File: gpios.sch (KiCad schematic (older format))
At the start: 13 parts

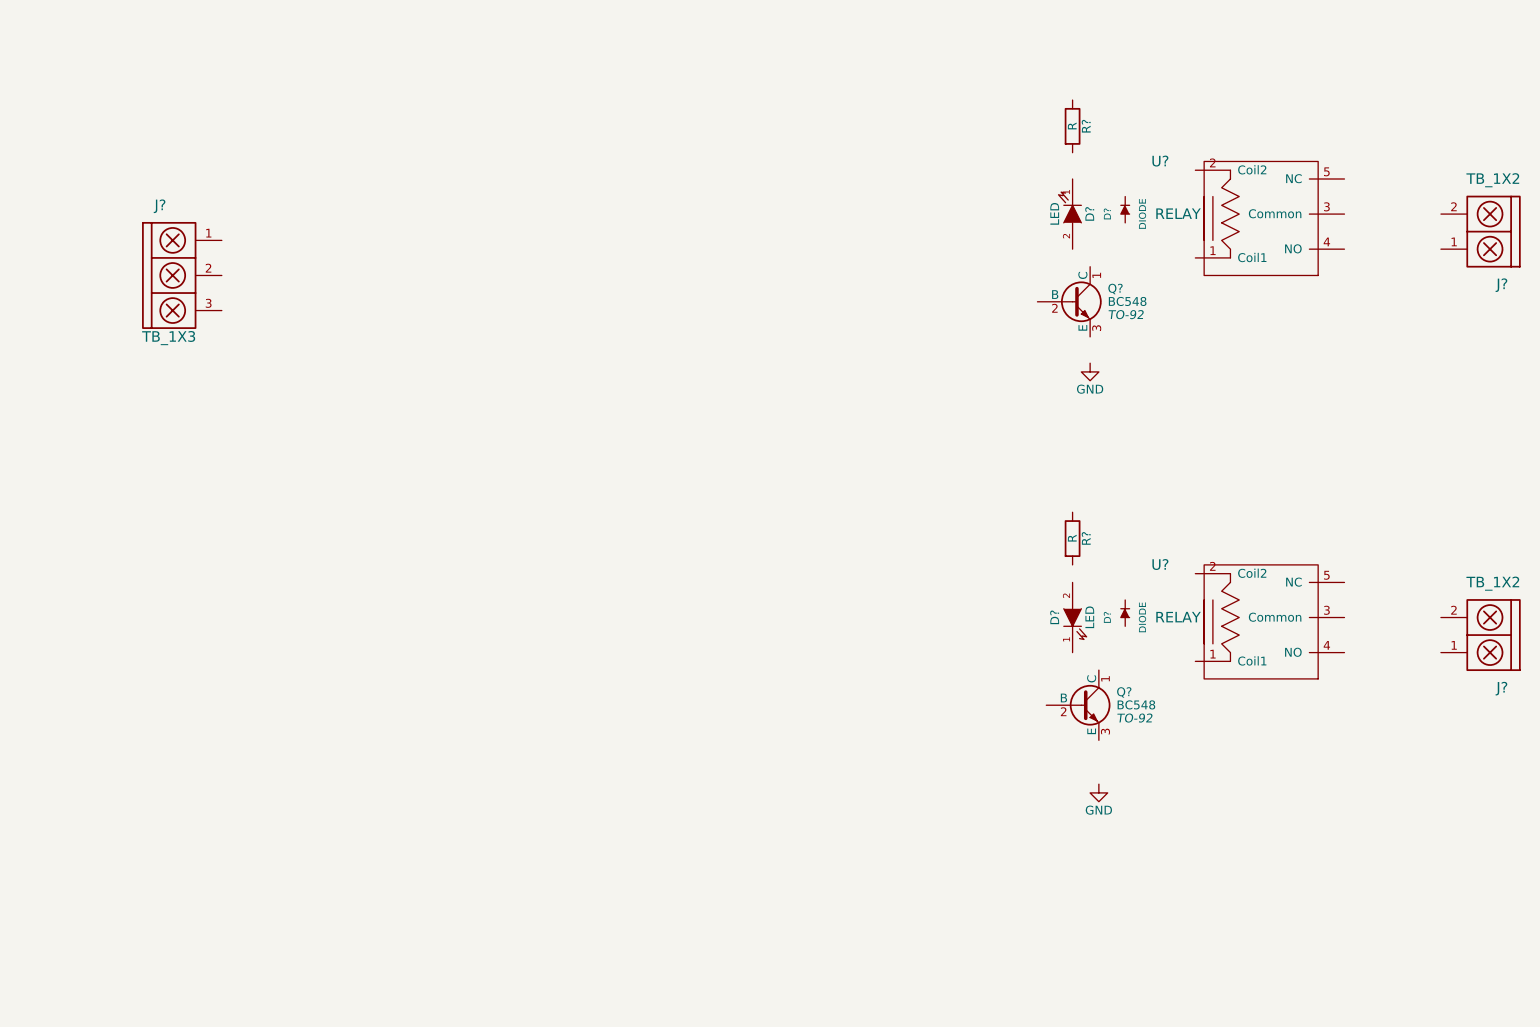
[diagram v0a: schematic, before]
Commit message: se creo componente RN1810 y LM35, se comenzo esquematico
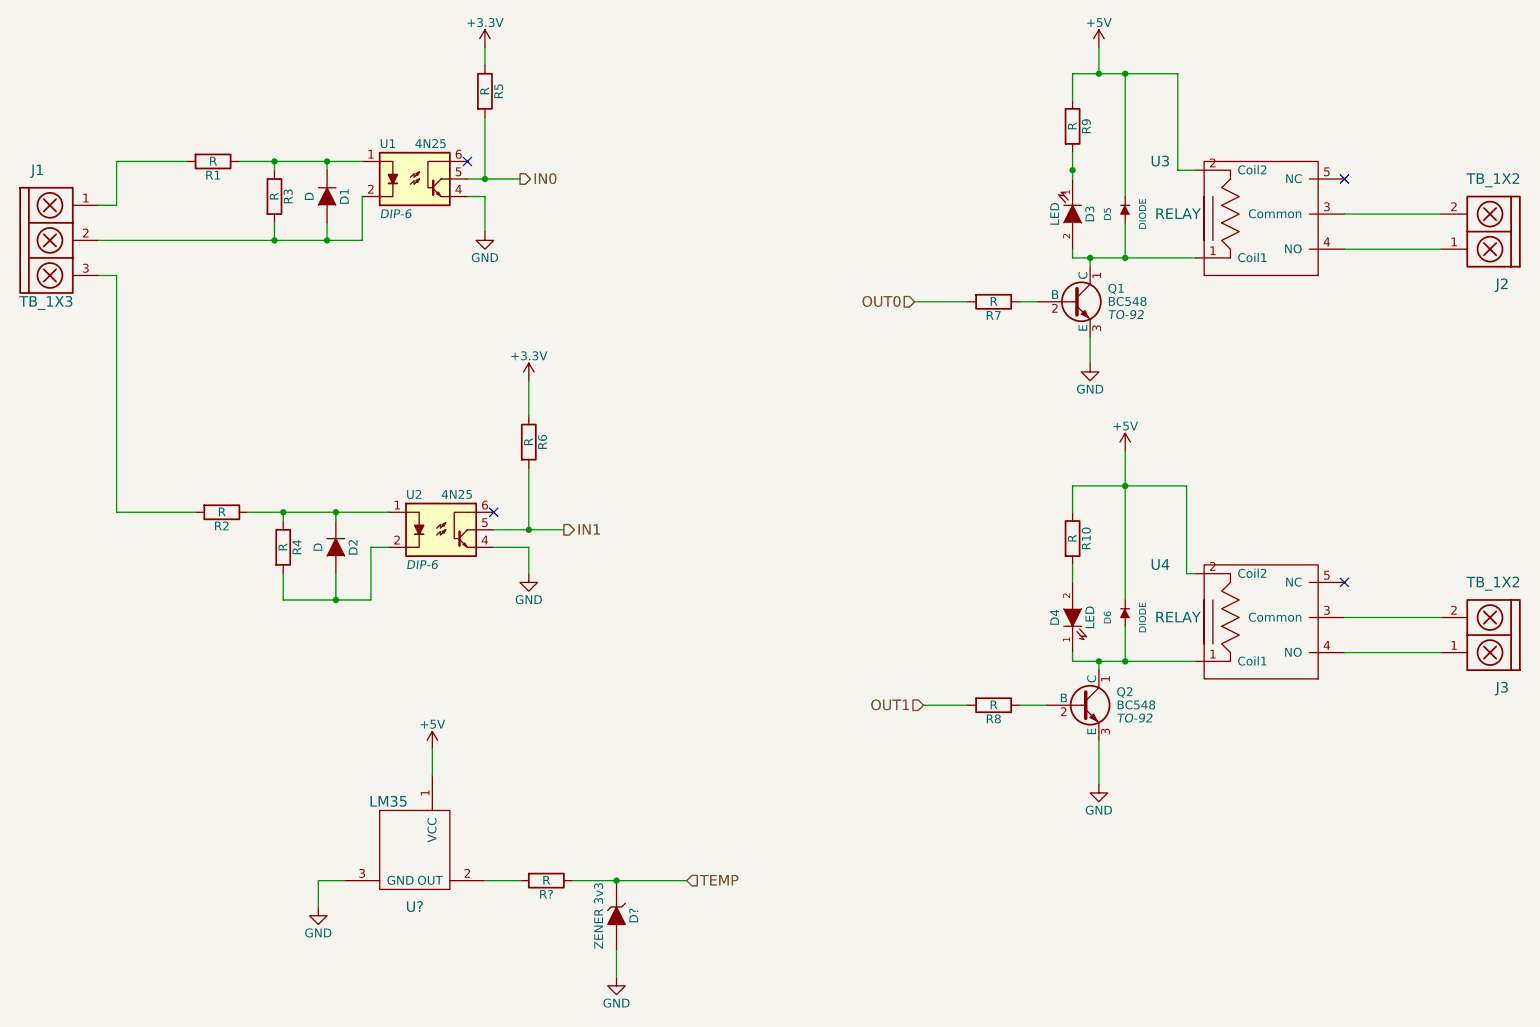
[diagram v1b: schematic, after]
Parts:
- added D1, D2: D, symbol D
- added D?: ZENER 3v3, symbol ZENER
- added R1, R2, R3, R4, R5, R6, R7, R8, R?: R, symbol R
- added U1, U2: 4N25, DIP-6, symbol 4N25
- added U?: LM35, symbol LM35
- gave numbers to parts that had none: 13
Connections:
- net GND: now also Q1.3 (E), Q2.3 (E), D?.2 (A), U1.4, U2.4, U?.3 (GND)
- net at J1.1: now also R1.2
- net at J1.2: now also D1.2 (A), R3.2, U1.2
- net at J1.3: now also R2.2
- net at J2.1: now also U3.4 (NO)
- net at J2.2: now also U3.3 (Common)
- net at J3.1: now also U4.4 (NO)
- net at J3.2: now also U4.3 (Common)
- net at U3.1 (Coil1): now also D3.2 (A), D5.1 (A), Q1.1 (C)
- net +5V: now reaches U3.2 (Coil2)
- net +5V: now also D5.2 (K), D6.2 (K), R10.1, R9.1, U4.2 (Coil2), U?.1 (VCC)
- net at U4.1 (Coil1): now also D4.1 (K), D6.1 (A), Q2.1 (C)
- net at Q1.2 (B): now also R7.1
- net at Q2.2 (B): now also R8.1
- net at D3.1 (K): now also R9.2
- net at D4.2 (A): now also R10.2
- new net: D1.1 (K), R1.1, R3.1, U1.1
- new net: D2.1 (K), R2.1, R4.1, U2.1
- new net: D2.2 (A), R4.2, U2.2
- new net: R?.2, U?.2 (OUT)
- new net +3V3: R5.1, R6.1
- new net IN0: R5.2, U1.5
- new net IN1: R6.2, U2.5
- new net OUT0: R7.2
- new net OUT1: R8.2
- new net TEMP: D?.1 (K), R?.1
- no-connect marks 0 -> 4
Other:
- moved on the sheet: J1

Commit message: se agrego conector de poncho
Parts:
- gave numbers to parts that had none: 3
- renumbered D3 to D4, D4 to D5, D5 to D6, D6 to D7, R9 to R10, R10 to R11, R7 to R8, R8 to R9, U2 to U3, U3 to U4, U4 to U5
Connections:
- net GND: no longer D3.2 (A), U2.3 (GND)
- new net GNDA: D3.2 (A), U2.3 (GND)
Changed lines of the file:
@@
 LIBS:lm35
 LIBS:rn1810e
+LIBS:Poncho_Esqueleto
 LIBS:ponchoeduciaaiot-cache
 EELAYER 25 0
@@
 $Descr A4 11693 8268
 encoding utf-8
-Sheet 2 3
+Sheet 2 4
 Title "Poncho EDU-CIAA-NXP IoT"
 Date "2016-11-09"
@@
 $EndComp
 $Comp
-L RELAY U3
+L RELAY U4
 U 1 1 5825F23B
 P 7700 1650
-F 0 "U3" H 7700 1650 60  0000 C CNN
+F 0 "U4" H 7700 1650 60  0000 C CNN
 F 1 "RELAY" H 7600 1950 60  0000 C CNN
 F 2 "" H 7700 1650 60  0001 C CNN
@@
 $EndComp
 $Comp
-L RELAY U4
+L RELAY U5
 U 1 1 5825F324
 P 7700 3950
-F 0 "U4" H 7700 3950 60  0000 C CNN
+F 0 "U5" H 7700 3950 60  0000 C CNN
 F 1 "RELAY" H 7600 4250 60  0000 C CNN
 F 2 "" H 7700 3950 60  0001 C CNN
@@
 $EndComp
 $Comp
-L DIODE D5
+L DIODE D6
 U 1 1 58260067
 P 7500 1950
-F 0 "D5" H 7500 2050 40  0000 C CNN
+F 0 "D6" H 7500 2050 40  0000 C CNN
 F 1 "DIODE" H 7500 1850 40  0000 C CNN
 F 2 "" H 7500 1950 60  0000 C CNN
@@
 $EndComp
 $Comp
-L DIODE D6
+L DIODE D7
 U 1 1 582601C2
 P 7500 4250
-F 0 "D6" H 7500 4350 40  0000 C CNN
+F 0 "D7" H 7500 4350 40  0000 C CNN
 F 1 "DIODE" H 7500 4150 40  0000 C CNN
 F 2 "" H 7500 4250 60  0000 C CNN
@@
 $EndComp
 $Comp
-L LED D3
+L LED D4
 U 1 1 58260865
 P 7200 1950
-F 0 "D3" H 7200 2050 50  0000 C CNN
+F 0 "D4" H 7200 2050 50  0000 C CNN
 F 1 "LED" H 7200 1850 50  0000 C CNN
 F 2 "" H 7200 1950 50  0000 C CNN
@@
 $EndComp
 $Comp
-L LED D4
+L LED D5
 U 1 1 5826096C
 P 7200 4250
-F 0 "D4" H 7200 4350 50  0000 C CNN
+F 0 "D5" H 7200 4350 50  0000 C CNN
 F 1 "LED" H 7200 4150 50  0000 C CNN
 F 2 "" H 7200 4250 50  0000 C CNN
@@
 $EndComp
 $Comp
-L R R9
+L R R10
 U 1 1 58260D12
 P 7200 1450
-F 0 "R9" V 7280 1450 50  0000 C CNN
+F 0 "R10" V 7280 1450 50  0000 C CNN
 F 1 "R" V 7200 1450 50  0000 C CNN
 F 2 "" V 7130 1450 50  0000 C CNN
@@
 $EndComp
 $Comp
-L R R10
+L R R11
 U 1 1 58260E67
 P 7200 3800
-F 0 "R10" V 7280 3800 50  0000 C CNN
+F 0 "R11" V 7280 3800 50  0000 C CNN
 F 1 "R" V 7200 3800 50  0000 C CNN
 F 2 "" V 7130 3800 50  0000 C CNN
@@
 	9300 4450 8750 4450
 $Comp
-L R R7
+L R R8
 U 1 1 58250D49
 P 6750 2450
-F 0 "R7" V 6830 2450 50  0000 C CNN
+F 0 "R8" V 6830 2450 50  0000 C CNN
 F 1 "R" V 6750 2450 50  0000 C CNN
 F 2 "" V 6680 2450 50  0000 C CNN
@@
 $EndComp
 $Comp
-L R R8
+L R R9
 U 1 1 58250E98
 P 6750 4750
-F 0 "R8" V 6830 4750 50  0000 C CNN
+F 0 "R9" V 6830 4750 50  0000 C CNN
 F 1 "R" V 6750 4750 50  0000 C CNN
 F 2 "" V 6680 4750 50  0000 C CNN
@@
 $EndComp
 $Comp
-L 4N25 U2
+L 4N25 U3
 U 1 1 58251FA6
 P 3600 3750
-F 0 "U2" H 3400 3950 50  0000 L CNN
+F 0 "U3" H 3400 3950 50  0000 L CNN
 F 1 "4N25" H 3600 3950 50  0000 L CNN
 F 2 "DIP-6" H 3400 3550 50  0000 L CIN
@@
 	6600 2450 6300 2450
 $Comp
-L LM35 U?
+L LM35 U2
 U 1 1 58262178
 P 3450 5900
-F 0 "U?" H 3450 5900 60  0000 C CNN
+F 0 "U2" H 3450 5900 60  0000 C CNN
 F 1 "LM35" H 3300 6500 60  0000 C CNN
 F 2 "" H 3450 5900 60  0001 C CNN
@@
 Wire Wire Line
 	3550 5000 3550 5150
-$Comp
-L GND #PWR010
-U 1 1 58262922
-P 2900 5900
-F 0 "#PWR010" H 2900 5650 50  0001 C CNN
-F 1 "GND" H 2900 5750 50  0000 C CNN
-F 2 "" H 2900 5900 50  0000 C CNN
-F 3 "" H 2900 5900 50  0000 C CNN
-	1    2900 5900
-	1    0    0    -1
-$EndComp
 Wire Wire Line
 	3050 5750 2900 5750
@@
 	2900 5750 2900 5900
 $Comp
-L R R?
+L R R7
 U 1 1 58263063
 P 4200 5750
-F 0 "R?" V 4280 5750 50  0000 C CNN
+F 0 "R7" V 4280 5750 50  0000 C CNN
 F 1 "R" V 4200 5750 50  0000 C CNN
 F 2 "" V 4130 5750 50  0000 C CNN
@@
 $EndComp
 $Comp
-L ZENER D?
+L ZENER D3
 U 1 1 582630C0
 P 4600 5950
-F 0 "D?" H 4600 6050 50  0000 C CNN
+F 0 "D3" H 4600 6050 50  0000 C CNN
 F 1 "ZENER 3v3" H 4600 5850 50  0000 C CNN
 F 2 "" H 4600 5950 50  0000 C CNN
@@
 	0    1    1    0
 $EndComp
-$Comp
-L GND #PWR011
-U 1 1 58263137
-P 4600 6300
-F 0 "#PWR011" H 4600 6050 50  0001 C CNN
-F 1 "GND" H 4600 6150 50  0000 C CNN
-F 2 "" H 4600 6300 50  0000 C CNN
-F 3 "" H 4600 6300 50  0000 C CNN
-	1    4600 6300
-	1    0    0    -1
-$EndComp
 Wire Wire Line
 	3850 5750 4050 5750
@@
 Text HLabel 5000 5750 2    60   Input ~ 0
 TEMP
+$Comp
+L GNDA #PWR010
+U 1 1 582671B3
+P 4600 6300
+F 0 "#PWR010" H 4600 6050 50  0001 C CNN
+F 1 "GNDA" H 4600 6150 50  0000 C CNN
+F 2 "" H 4600 6300 50  0000 C CNN
+F 3 "" H 4600 6300 50  0000 C CNN
+	1    4600 6300
+	1    0    0    -1
+$EndComp
+$Comp
+L GNDA #PWR011
+U 1 1 582671FF
+P 2900 5900
+F 0 "#PWR011" H 2900 5650 50  0001 C CNN
+F 1 "GNDA" H 2900 5750 50  0000 C CNN
+F 2 "" H 2900 5900 50  0000 C CNN
+F 3 "" H 2900 5900 50  0000 C CNN
+	1    2900 5900
+	1    0    0    -1
+$EndComp
 $EndSCHEMATC
